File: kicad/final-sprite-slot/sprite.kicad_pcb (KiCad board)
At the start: 4 copper layers, 35 x 44.6 mm, 66 parts, among them J1 M20-7910442R, U1 CC430F513X, U2 LSM9DS1, U3 SPRITETCXO_TCXO_7Z, U4 DRV8837, U5 ADP5092, U6 DRV8837, U7 DRV8837, X1 SPRITEPIN_SPRITE_PIN, X2 SPRITEPIN_SPRITE_PIN

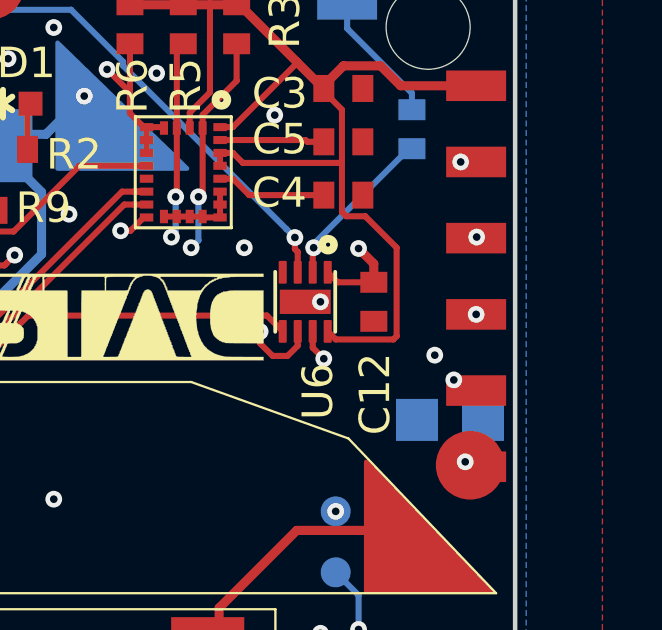
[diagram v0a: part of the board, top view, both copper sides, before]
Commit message: added in new super cap
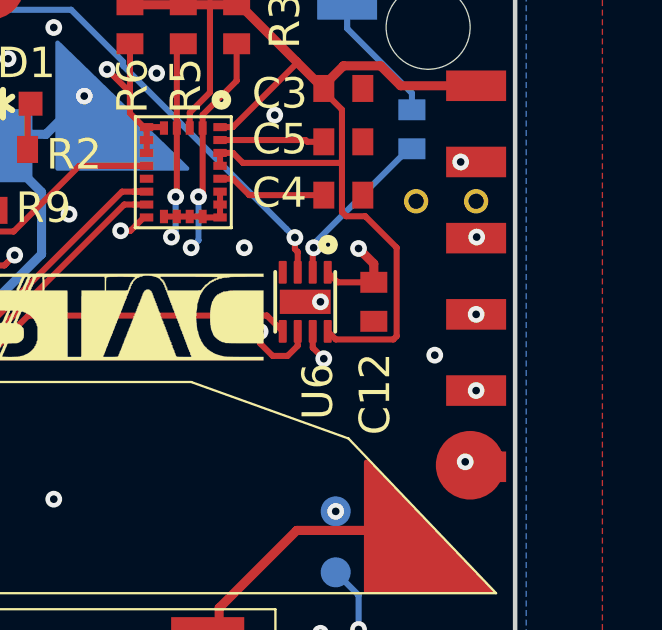
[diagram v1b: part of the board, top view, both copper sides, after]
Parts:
- removed C10: CPH3225A, CAPCP3225X100N
- added B1: UMAC_UMAC, sprite:UMAC_UMAC, B.Cu at (153.5, 94.7)
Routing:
- net /UART_RX: track 23.9 -> 24.8 mm
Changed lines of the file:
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@@
-(kicad_pcb (version 20171130) (host pcbnew 6.0.0-rc1-unknown-3eb3db0~66~ubuntu16.04.1)
+(kicad_pcb (version 20171130) (host pcbnew "(5.0.0-rc2-225-g4af699e91)")
   (general
     (thickness 0.7874)
     (drawings 25)
-    (tracks 985)
+    (tracks 984)
     (zones 0)
     (modules 66)
-    (nets 72)
+    (nets 70)
   )
   (page USLetter)
@@
     (31 Bottom signal)
     (32 B.Adhes user)
-    (33 F.Adhes user hide)
+    (33 F.Adhes user)
     (34 B.Paste user)
     (35 F.Paste user)
@@
     (zone_45_only no)
     (trace_min 0.1524)
+    (segment_width 0.15)
+    (edge_width 0.15)
     (via_size 0.5588)
     (via_drill 0.254)
@@
     (uvia_min_size 0.2)
     (uvia_min_drill 0.1)
-    (edge_width 0.15)
-    (segment_width 0.15)
     (pcb_text_width 0.3)
     (pcb_text_size 1.5 1.5)
@@
   (net 68 "Net-(U1-Pad47)")
   (net 69 "Net-(U1-Pad17)")
-  (net 70 "Net-(C10-Pad2)")
-  (net 71 "Net-(C10-Pad1)")
   (net_class Default "This is the default net class."
     (clearance 0.1524)
@@
     (uvia_dia 25.4)
     (uvia_drill 12.7)
-    (diff_pair_width 0.1524)
     (diff_pair_gap 0.1524)
+    (diff_pair_width 0.1524)
     (add_net /DRDY)
     (add_net /DSW)
@@
     (add_net /~RST)
     (add_net GND)
-    (add_net "Net-(C10-Pad1)")
-    (add_net "Net-(C10-Pad2)")
     (add_net "Net-(C4-Pad1)")
     (add_net "Net-(C5-Pad1)")
@@
     (uvia_dia 25.4)
     (uvia_drill 12.7)
-    (diff_pair_width 0.1524)
     (diff_pair_gap 0.1524)
+    (diff_pair_width 0.1524)
     (add_net /SWN)
     (add_net /VBAT)
@@
     (add_net VCCIO)
   )
-  (module CAPCP3225X100N (layer Bottom)
-    (at 153.67 99.441)
-    (fp_text reference C10 (at -1.50651 1.50651) (layer B.SilkS)
-      (effects (font (size 0.58163 0.58163) (thickness 0.048979)) (justify left bottom mirror))
-    )
-    (fp_text value CPH3225A (at -1.50112 -2.25168) (layer B.Fab)
-      (effects (font (size 0.579552 0.579552) (thickness 0.048804)) (justify left bottom mirror))
-    )
-    (fp_line (start 1.6 -1.25) (end -1.6 -1.25) (layer B.Fab) (width 0.127))
-    (fp_line (start -1.6 -1.25) (end -1.6 1.25) (layer B.Fab) (width 0.127))
-    (fp_line (start -1.6 1.25) (end 1.6 1.25) (layer B.Fab) (width 0.127))
-    (fp_line (start 1.6 1.25) (end 1.6 -1.25) (layer B.Fab) (width 0.127))
-    (fp_line (start 1.6 -1) (end 1.6 -1.25) (layer B.SilkS) (width 0.127))
-    (fp_line (start 1.6 -1.25) (end -1.6 -1.25) (layer B.SilkS) (width 0.127))
-    (fp_line (start -1.6 -1.25) (end -1.6 -1) (layer B.SilkS) (width 0.127))
-    (fp_line (start 1.6 1) (end 1.6 1.25) (layer B.SilkS) (width 0.127))
-    (fp_line (start 1.6 1.25) (end -1.6 1.25) (layer B.SilkS) (width 0.127))
-    (fp_line (start -1.6 1.25) (end -1.6 1) (layer B.SilkS) (width 0.127))
-    (fp_line (start 2.05 -1.5) (end -2.05 -1.5) (layer Dwgs.User) (width 0.05))
-    (fp_line (start -2.05 -1.5) (end -2.05 1.5) (layer Dwgs.User) (width 0.05))
-    (fp_line (start -2.05 1.5) (end 2.05 1.5) (layer Dwgs.User) (width 0.05))
-    (fp_line (start 2.05 1.5) (end 2.05 -1.5) (layer Dwgs.User) (width 0.05))
-    (fp_circle (center -2.25 1) (end -2.15 1) (layer B.SilkS) (width 0.2))
-    (pad 2 smd rect (at 1.1 0 180) (size 1.4 1.4) (layers Bottom B.Paste B.Mask)
-      (net 70 "Net-(C10-Pad2)") (solder_mask_margin 0.1016))
-    (pad 1 smd rect (at -1.1 0 180) (size 1.4 1.4) (layers Bottom B.Paste B.Mask)
-      (net 71 "Net-(C10-Pad1)") (solder_mask_margin 0.1016))
-  )
   (module sprite:R0402 (layer Top)
     (at 122.555 98.552)
@@
       (net 64 "Net-(L3-Pad1)") (solder_mask_margin 0.1016))
   )
+  (module sprite:UMAC_UMAC (layer Bottom)
+    (at 153.5411 94.652074 90)
+    (fp_text reference B1 (at 0 0 90) (layer B.SilkS) hide
+      (effects (font (size 1.27 1.27) (thickness 0.15)) (justify mirror))
+    )
+    (fp_text value UMAC_UMAC (at 0 0 90) (layer B.SilkS) hide
+      (effects (font (size 1.27 1.27) (thickness 0.15)) (justify mirror))
+    )
+    (fp_text user - (at 1.016 -1.016 90) (layer B.SilkS)
+      (effects (font (size 1 1) (thickness 0.15)) (justify mirror))
+    )
+    (fp_text user + (at 1.016 1.016 90) (layer B.SilkS)
+      (effects (font (size 1 1) (thickness 0.15)) (justify mirror))
+    )
+    (fp_line (start 0 -2.032) (end 0 2.032) (layer B.SilkS) (width 0.15))
+    (fp_line (start -12.065 -2.032) (end 0 -2.032) (layer B.SilkS) (width 0.15))
+    (fp_line (start -12.065 2.032) (end -12.065 -2.032) (layer B.SilkS) (width 0.15))
+    (fp_line (start 0 2.032) (end -12.065 2.032) (layer B.SilkS) (width 0.15))
+    (fp_line (start -12.192 -2.159) (end -12.192 2.159) (layer B.CrtYd) (width 0.15))
+    (fp_line (start 3.175 -2.159) (end -12.192 -2.159) (layer B.CrtYd) (width 0.15))
+    (fp_line (start 3.175 2.159) (end 3.175 -2.159) (layer B.CrtYd) (width 0.15))
+    (fp_line (start -12.192 2.159) (end 3.175 2.159) (layer B.CrtYd) (width 0.15))
+    (pad V- thru_hole circle (at 2.5 -1 90) (size 0.8128 0.8128) (drill 0.508) (layers *.Cu *.Mask)
+      (net 2 GND) (solder_mask_margin 0.1016))
+    (pad V+ thru_hole circle (at 2.5 1 90) (size 0.8128 0.8128) (drill 0.508) (layers *.Cu *.Mask)
+      (net 23 /VBAT) (solder_mask_margin 0.1016))
+  )
   (module sprite:SPRITEPIN_SPRITE_PIN (layer Top)
     (at 138.3411 84.952074)
@@
   (segment (start 133.997155 90.678) (end 138.034 90.678) (width 0.2032) (layer Top) (net 53) (status 20))
   (segment (start 133.100898 91.574257) (end 133.997155 90.678) (width 0.2032) (layer Top) (net 53) (status 10))
-  (via (at 153.797 98.1075) (size 0.5588) (drill 0.254) (layers Top Bottom) (net 54) (status 30))
+  (via (at 154.5411 98.462074) (size 0.5588) (drill 0.254) (layers Top Bottom) (net 54) (status 30))
   (via (at 134.309429 97.304922) (size 0.5588) (drill 0.254) (layers Top Bottom) (net 54))
   (segment (start 131.333131 94.897658) (end 131.333131 95.039575) (width 0.2032) (layer Top) (net 54))
@@
   (segment (start 133.319079 97.025523) (end 134.03003 97.025523) (width 0.2032) (layer Top) (net 54))
   (segment (start 134.03003 97.025523) (end 134.309429 97.304922) (width 0.2032) (layer Top) (net 54))
-  (segment (start 149.380422 98.1075) (end 153.401869 98.1075) (width 0.2032) (layer Route3) (net 54))
-  (segment (start 148.612922 97.34) (end 149.380422 98.1075) (width 0.2032) (layer Route3) (net 54))
-  (segment (start 148.612922 97.304922) (end 148.612922 97.34) (width 0.2032) (layer Route3) (net 54))
-  (segment (start 153.401869 98.1075) (end 153.797 98.1075) (width 0.2032) (layer Route3) (net 54))
-  (segment (start 134.309429 97.304922) (end 148.612922 97.304922) (width 0.2032) (layer Route3) (net 54))
+  (segment (start 149.770074 98.462074) (end 148.612922 97.304922) (width 0.2032) (layer Route3) (net 54))
+  (segment (start 134.70456 97.304922) (end 134.309429 97.304922) (width 0.2032) (layer Route3) (net 54))
+  (segment (start 154.5411 98.462074) (end 149.770074 98.462074) (width 0.2032) (layer Route3) (net 54))
+  (segment (start 148.612922 97.304922) (end 134.70456 97.304922) (width 0.2032) (layer Route3) (net 54))
   (via (at 154.5411 95.922074) (size 0.5588) (drill 0.254) (layers Top Bottom) (net 55) (status 30))
   (segment (start 131.330992 95.602626) (end 131.330992 95.791793) (width 0.2032) (layer Top) (net 55) (status 10))

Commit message: umac cutout spot
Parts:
- J1: moved to B.Cu
- moved B1 8.50 mm to (149.9, 87.0)
- moved L4 0.21 mm to (141.1, 84.7)
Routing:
- net /TST: track 54.3 -> 2.41 mm, vias 2 -> 1
- net /VBAT: track 25.6 -> 19.5 mm
- net VCC: track 138.1 -> 132.5 mm
- net Net-(U1-Pad47): track 1.51 -> 0.14 mm, vias 1 -> 0
- net VCCIO: vias 5 -> 4
- net Net-(R12-Pad1): vias 1 -> 0
- net Net-(L4-Pad2): vias 1 -> 0
- net GND: vias 29 -> 27
- net /EN_2: vias 2 -> 1
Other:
- outline, holes or cut-outs redrawn

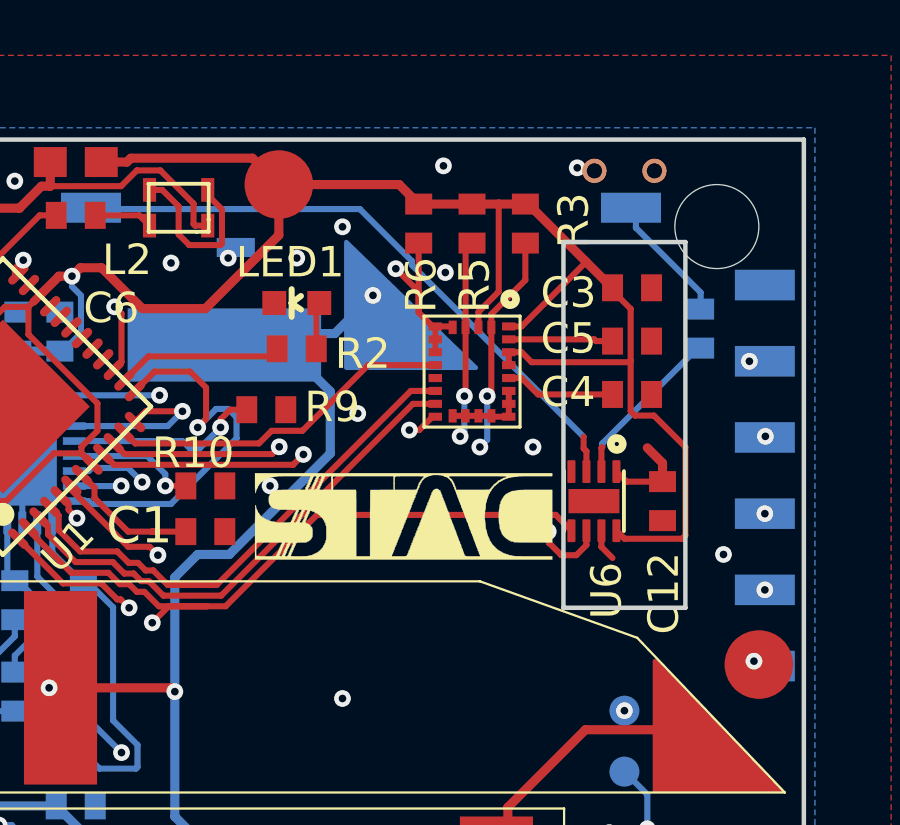
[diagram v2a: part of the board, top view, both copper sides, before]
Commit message: moving some passives
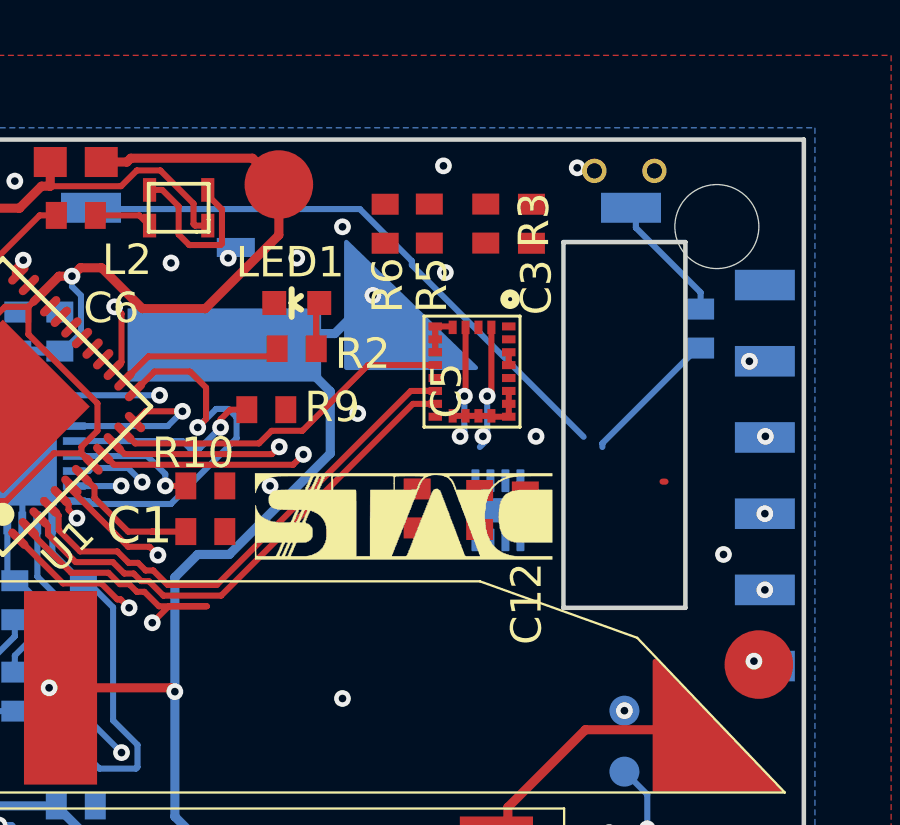
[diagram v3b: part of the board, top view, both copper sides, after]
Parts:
- U6: moved to B.Cu
- moved C4 8.11 mm to (143.0, 95.7), turned to 270 degrees
- moved C5 7.58 mm to (145.0, 95.8), turned to 270 degrees
- moved C12 4.59 mm to (146.6, 95.8)
- moved C3 3.97 mm to (146.8, 86.3), turned to 90 degrees
- moved U6 3.21 mm to (145.6, 95.8), turned to 90 degrees
- moved R5 1.42 mm to (143.4, 86.3)
- moved R3 1.32 mm to (145.2, 86.3)
- moved R6 1.12 mm to (141.9, 86.3)
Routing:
- net VCC: track 132.5 -> 95.7 mm
- net /PWM1: track 41.3 -> 22.8 mm, vias 4 -> 3
- net /PWM2: track 39.1 -> 25.4 mm
- net Net-(R6-Pad2): track 12.9 -> 1.45 mm, vias 2 -> 0
- net Net-(C4-Pad1): track 3.69 -> 0.00 mm
- net Net-(C5-Pad1): track 3.48 -> 0.00 mm
- net /SCL: track 20.8 -> 17.6 mm
- net VCCIO: track 78.9 -> 75.9 mm
- net /SDA: track 19.2 -> 16.3 mm
- net Net-(L4-Pad2): track 20.7 -> 19.5 mm
- net /EN_2: track 26.4 -> 25.3 mm
- net Net-(R12-Pad1): track 5.54 -> 4.71 mm

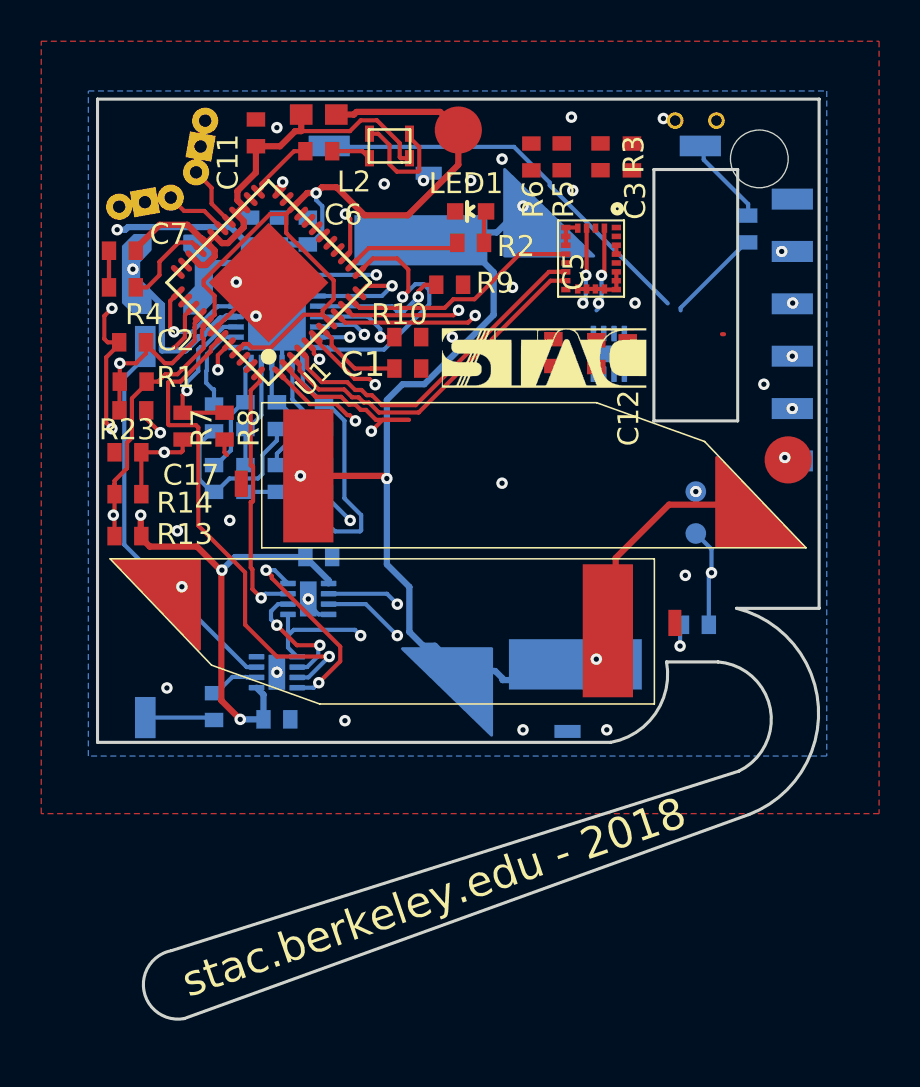
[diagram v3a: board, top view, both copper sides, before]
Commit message: WIP routing w slot
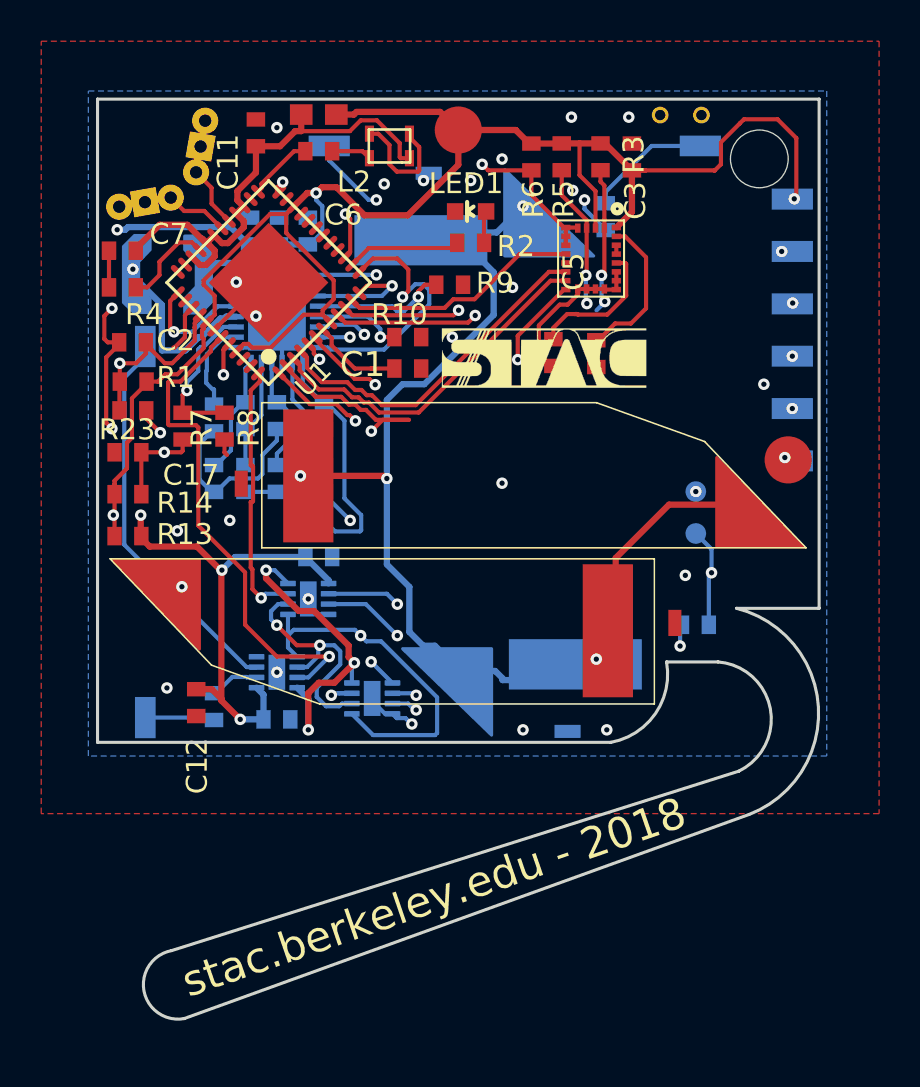
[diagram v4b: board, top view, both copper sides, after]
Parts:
- moved C12 26.9 mm to (125.6, 112.7)
- moved U6 20.3 mm to (134.2, 112.5), turned to 180 degrees
- moved R12 6.93 mm to (145.5, 89.2)
- moved B1 0.78 mm to (149.1, 86.7)
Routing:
- net Net-(R22-Pad1): track 736.5 -> 555.1 mm
- net VCC: track 95.7 -> 132.1 mm, vias 4 -> 6
- net Net-(R12-Pad1): track 4.71 -> 32.9 mm, vias 0 -> 2
- net Net-(R6-Pad2): track 1.45 -> 28.3 mm, vias 0 -> 2
- net Net-(L4-Pad2): track 19.5 -> 34.8 mm, vias 0 -> 2
- net /VBAT: track 19.5 -> 4.76 mm
- net /PWM2: track 25.4 -> 36.7 mm
- net VCCIO: track 75.9 -> 67.9 mm, vias 4 -> 5
- net GND: track 38.2 -> 45.9 mm, vias 27 -> 26
- net Net-(C5-Pad1): track 0.00 -> 7.39 mm
- net Net-(C4-Pad1): track 0.00 -> 6.94 mm
- net /PWM1: track 22.8 -> 28.6 mm
- net /EN_2: track 25.3 -> 21.4 mm, vias 1 -> 2
- net /SCL: track 17.6 -> 21.1 mm
- net /SDA: track 16.3 -> 19.5 mm
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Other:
- outline, holes or cut-outs redrawn

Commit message: WIP more routing
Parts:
- B1: moved to F.Cu
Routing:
- net /UART_TX: track 24.7 -> 1.08 mm
- net /UART_RX: track 24.8 -> 4.06 mm
